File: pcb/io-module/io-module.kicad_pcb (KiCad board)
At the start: 4 copper layers, 50 x 25 mm, 128 parts, among them J1 SWD Header, SW1 SKRPABE010, U1 STM32C051G8Ux, Y1 ECS-480-10-37B2-RWN-TR

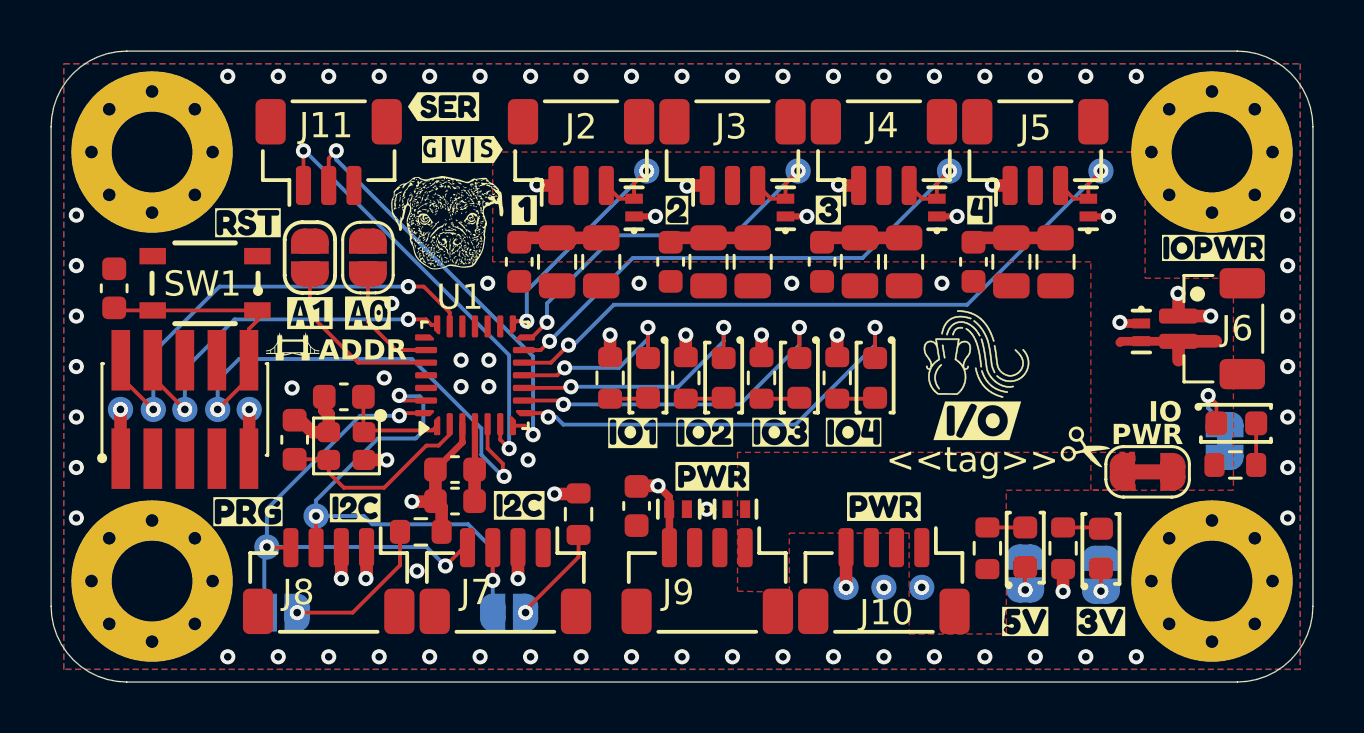
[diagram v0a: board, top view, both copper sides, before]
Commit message: Updated parts and IO power connection
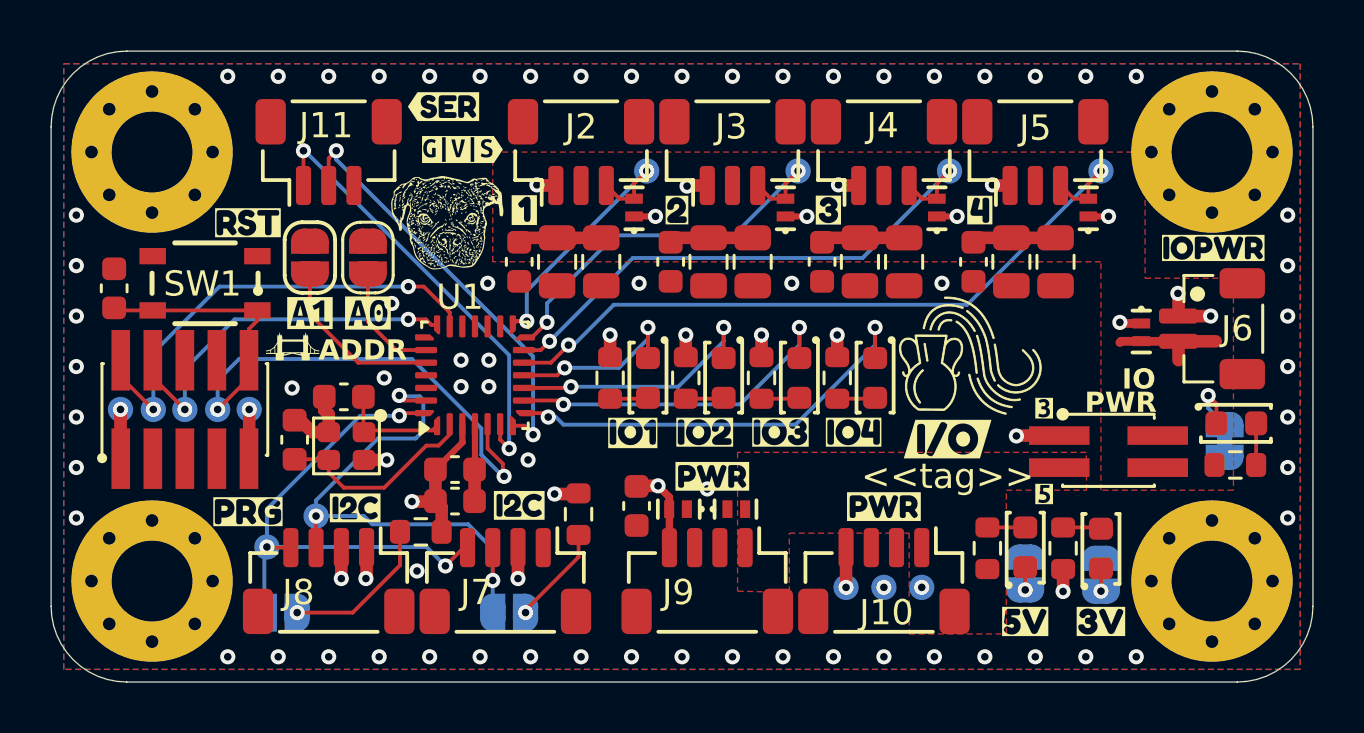
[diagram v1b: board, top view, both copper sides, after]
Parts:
- removed JP5: ~, CRGM Connector:SolderJumper-2_P2.0mm_Bridged_RoundedPad1.0x1.5mm
- removed kibuzzard-6A2A3A1C: G***, kibuzzard-6A2A3A1C
- removed kibuzzard-6A2A3A22: G***, kibuzzard-6A2A3A22
- removed kibuzzard-6A2A3A2A: G***, kibuzzard-6A2A3A2A
- removed kibuzzard-6A2A3A2F: G***, kibuzzard-6A2A3A2F
- added J12: Conn_02x02_Odd_Even, CRGM Connector:PinHeader_2x02_P1.27mm_Vertical_SMD, F.Cu at (91.9, 100.9)
- added kibuzzard-6A72852B: G***, kibuzzard-6A72852B, B.Cu at (90.2, 88.3)
- added kibuzzard-6A728531: G***, kibuzzard-6A728531, B.Cu at (84.2, 88.3)
- added kibuzzard-6A728536: G***, kibuzzard-6A728536, B.Cu at (78.2, 88.2)
- added kibuzzard-6A72853D: G***, kibuzzard-6A72853D, B.Cu at (72.3, 88.2)
- added kibuzzard-6A728CD5: G***, kibuzzard-6A728CD5, F.Cu at (89.3, 102.5)
- added kibuzzard-6A728CE2: G***, kibuzzard-6A728CE2, F.Cu at (89.3, 99.2)
- JP1, JP2, JP3, JP4: value ~ -> SolderJumper_2_Open
- JP6, JP7, JP8: value ~ -> SolderJumper_2_Bridged
- LOGO2: footprint CRGM Logos:Aquarius Logo 3.5mm -> CRGM Logos:Aquarius Logo 5mm
- moved LOGO6 18.4 mm to (75.6, 105.7)
- moved LOGO4 15.5 mm to (60.6, 91.9)
- moved LOGO3 15.0 mm to (67.8, 91.6)
- moved LOGO1 4.81 mm to (89.0, 92.7)
- moved kibuzzard-6A727258 4.81 mm to (89.2, 95.6)
- moved kibuzzard-6A7271F3 1.38 mm to (85.5, 100.4)
- moved LOGO2 0.79 mm to (86.1, 97.5)
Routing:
- net +3.3V: track 20.4 -> 22.1 mm, vias 12 -> 13
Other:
- board text added: "Analog"
- board text added: "GPIO"
- board text added: "Other"
- board text added: "Relay"
- board text added: "Servo"
